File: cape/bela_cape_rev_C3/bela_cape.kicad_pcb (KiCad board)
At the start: 4 copper layers, 71.8 x 54.6 mm, 153 parts, among them IC1 PAM8406, IC2 TLV320AIC3104, IC3 MIC5317, IC4 MC33204, IC5 MC33204, IC6 ES9080Q, IC7 TSV524xIQ4T, IC8 TSV524xIQ4T, IC9 ADS8168, J1 Conn_01x02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

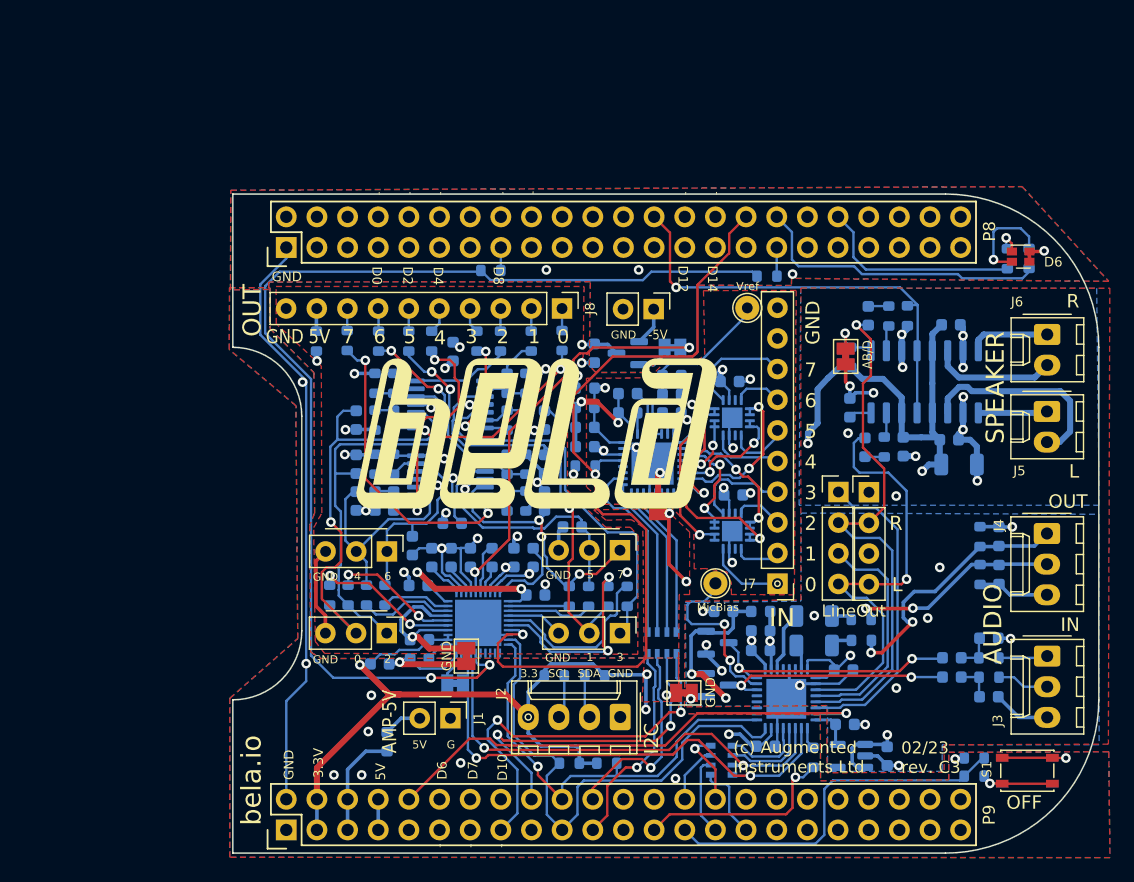
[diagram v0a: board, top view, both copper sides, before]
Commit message: Adding bela mini add-on footprint
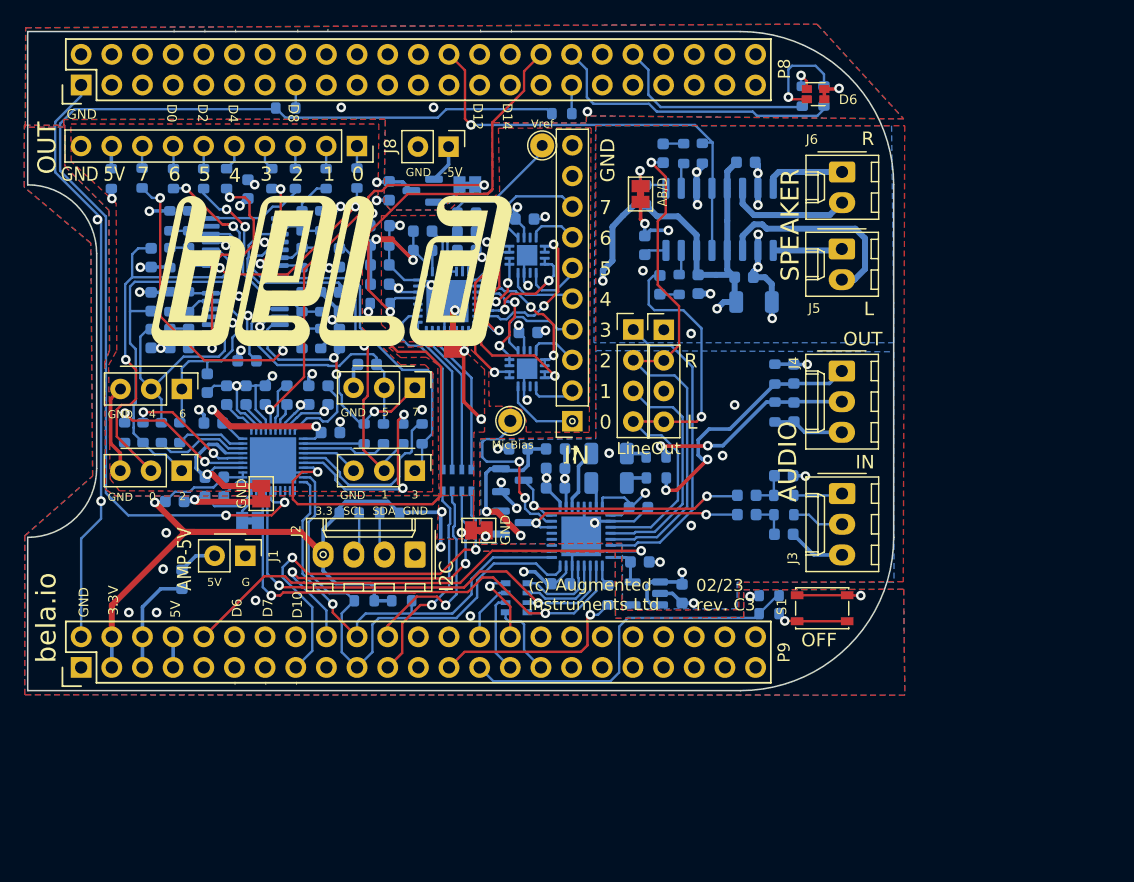
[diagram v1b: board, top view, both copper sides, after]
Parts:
- J7, J8: footprint Connector_PinHeader_2.54mm:PinHeader_1x10_P2.54mm_Vertical -> Connector_PinSocket_2.54mm:PinSocket_1x10_P2.54mm_Vertical
- moved C13 21.7 mm to (158.3, 106.0)
- moved C2 21.7 mm to (151.2, 85.2)
- moved C20 21.7 mm to (149.8, 110.9)
- moved C32 21.7 mm to (112.1, 94.4)
- moved C33 21.7 mm to (113.7, 94.4)
- moved C46 21.7 mm to (124.8, 82.0)
- moved C47 21.7 mm to (124.8, 85.2)
- moved C48 21.7 mm to (132.0, 82.4)
- moved C5 21.7 mm to (148.0, 85.3)
- moved D2 21.7 mm to (159.1, 95.8)
- moved D4 21.7 mm to (135.8, 105.0)
- moved D6 21.7 mm to (160.9, 69.5)
- moved FB1 21.7 mm to (108.4, 109.7)
- moved IC4 21.7 mm to (113.7, 81.7)
- moved IC5 21.7 mm to (113.7, 87.9)
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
